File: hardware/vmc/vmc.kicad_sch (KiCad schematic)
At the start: 37 parts, among them J1 Conn_01x05_Pin, J2 push button, J3 BUS, M1 F130, Q1 BSS123, U1 SHT31-DIS, U2 PIC18F05Q40, U4 MCP2003B, U5 uA7805, U6 MAX22201

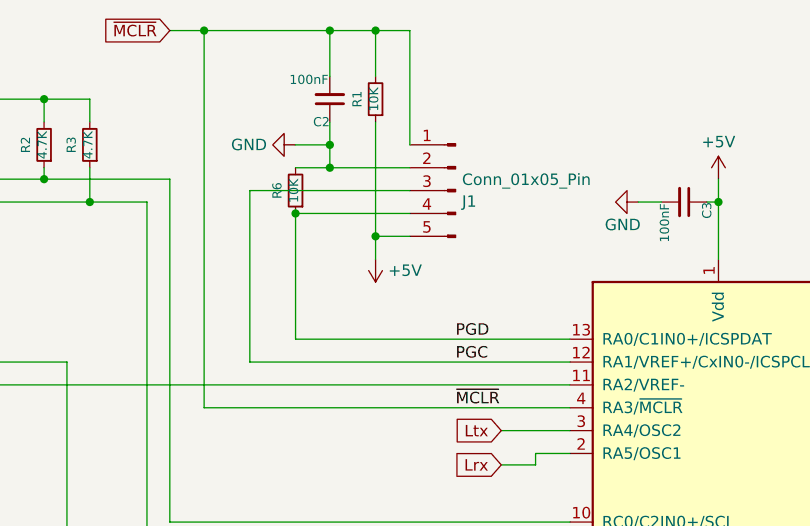
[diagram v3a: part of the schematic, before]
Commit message: vmc: update ICSP connector to match ventil
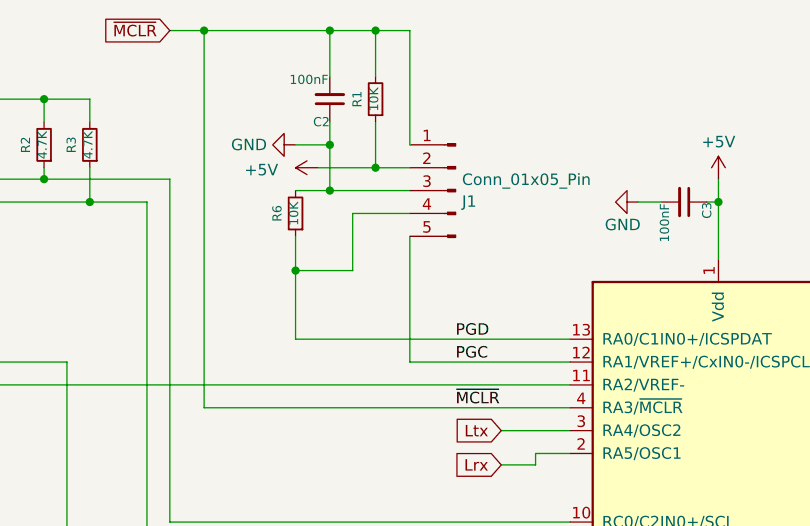
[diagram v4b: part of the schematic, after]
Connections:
- net +5V: now also J1.2 (Pin_2); no longer J1.5 (Pin_5)
- net GND: now also J1.3 (Pin_3); no longer J1.2 (Pin_2)
- net PGC: now also J1.5 (Pin_5); no longer J1.3 (Pin_3)
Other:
- moved on the sheet: R6
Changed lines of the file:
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@@
 	)
 	(junction
+		(at 201.93 38.1)
+		(diameter 0)
+		(color 0 0 0 0)
+	)
+	(junction
 		(at 73.66 161.29)
 		(diameter 0)
@@
 	)
 	(junction
-		(at 170.18 27.94)
+		(at 198.12 46.99)
 		(diameter 0)
 		(color 0 0 0 0)
 	)
 	(junction
-		(at 132.08 134.62)
+		(at 170.18 27.94)
 		(diameter 0)
 		(color 0 0 0 0)
 	)
 	(junction
-		(at 198.12 40.64)
+		(at 132.08 134.62)
 		(diameter 0)
 		(color 0 0 0 0)
@@
 	)
 	(junction
-		(at 207.01 43.18)
-		(diameter 0)
-		(color 0 0 0 0)
-	)
-	(junction
 		(at 86.36 161.29)
 		(diameter 0)
@@
 	)
 	(junction
-		(at 80.01 74.93)
+		(at 207.01 35.56)
 		(diameter 0)
 		(color 0 0 0 0)
 	)
 	(junction
-		(at 88.9 30.48)
+		(at 80.01 74.93)
 		(diameter 0)
 		(color 0 0 0 0)
 	)
 	(junction
-		(at 201.93 35.56)
+		(at 88.9 30.48)
 		(diameter 0)
 		(color 0 0 0 0)
@@
 	(wire
 		(pts
-			(xy 193.04 38.1) (xy 210.82 38.1)
-		)
-		(stroke
-			(width 0)
-			(type default)
-		)
-	)
-	(wire
-		(pts
 			(xy 86.36 161.29) (xy 86.36 163.83)
 		)
@@
 	(wire
 		(pts
-			(xy 193.04 57.15) (xy 193.04 38.1)
+			(xy 198.12 46.99) (xy 198.12 43.18)
 		)
 		(stroke
@@
 	(wire
 		(pts
-			(xy 210.82 43.18) (xy 207.01 43.18)
+			(xy 142.24 49.53) (xy 153.67 49.53)
 		)
 		(stroke
@@
 	(wire
 		(pts
-			(xy 142.24 49.53) (xy 153.67 49.53)
+			(xy 68.58 67.31) (xy 76.2 67.31)
 		)
 		(stroke
@@
 	(wire
 		(pts
-			(xy 68.58 67.31) (xy 76.2 67.31)
+			(xy 149.86 110.49) (xy 144.78 110.49)
 		)
 		(stroke
@@
 	(wire
 		(pts
-			(xy 149.86 110.49) (xy 144.78 110.49)
+			(xy 207.01 35.56) (xy 210.82 35.56)
 		)
 		(stroke
@@
 	(wire
 		(pts
-			(xy 198.12 54.61) (xy 198.12 40.64)
+			(xy 198.12 54.61) (xy 198.12 46.99)
 		)
 		(stroke
@@
 	(wire
 		(pts
+			(xy 204.47 40.64) (xy 204.47 46.99)
+		)
+		(stroke
+			(width 0)
+			(type default)
+		)
+	)
+	(wire
+		(pts
 			(xy 163.83 39.37) (xy 175.26 39.37)
 		)
@@
 	(wire
 		(pts
+			(xy 204.47 46.99) (xy 198.12 46.99)
+		)
+		(stroke
+			(width 0)
+			(type default)
+		)
+	)
+	(wire
+		(pts
 			(xy 109.22 53.34) (xy 111.76 53.34)
 		)
@@
 	(wire
 		(pts
-			(xy 228.6 57.15) (xy 193.04 57.15)
+			(xy 228.6 57.15) (xy 210.82 57.15)
 		)
 		(stroke
@@
 	(wire
 		(pts
+			(xy 201.93 38.1) (xy 210.82 38.1)
+		)
+		(stroke
+			(width 0)
+			(type default)
+		)
+	)
+	(wire
+		(pts
 			(xy 198.12 123.19) (xy 180.34 123.19)
 		)
@@
 	(wire
 		(pts
-			(xy 198.12 35.56) (xy 201.93 35.56)
+			(xy 198.12 38.1) (xy 201.93 38.1)
 		)
 		(stroke
@@
 	(wire
 		(pts
-			(xy 201.93 33.02) (xy 201.93 35.56)
+			(xy 201.93 33.02) (xy 201.93 38.1)
 		)
 		(stroke
@@
 	(wire
 		(pts
+			(xy 210.82 40.64) (xy 204.47 40.64)
+		)
+		(stroke
+			(width 0)
+			(type default)
+		)
+	)
+	(wire
+		(pts
 			(xy 142.24 72.39) (xy 152.4 72.39)
 		)
@@
 	(wire
 		(pts
-			(xy 207.01 30.48) (xy 207.01 43.18)
+			(xy 207.01 30.48) (xy 207.01 35.56)
 		)
 		(stroke
@@
 	(wire
 		(pts
-			(xy 228.6 80.01) (xy 172.72 80.01)
+			(xy 200.66 35.56) (xy 207.01 35.56)
 		)
 		(stroke
@@
 	(wire
 		(pts
-			(xy 76.2 46.99) (xy 88.9 46.99)
+			(xy 228.6 80.01) (xy 172.72 80.01)
 		)
 		(stroke
@@
 	(wire
 		(pts
-			(xy 198.12 40.64) (xy 210.82 40.64)
+			(xy 76.2 46.99) (xy 88.9 46.99)
 		)
 		(stroke
@@
 	(wire
 		(pts
-			(xy 201.93 35.56) (xy 210.82 35.56)
-		)
-		(stroke
-			(width 0)
-			(type default)
-		)
-	)
-	(wire
-		(pts
 			(xy 163.83 36.83) (xy 170.18 36.83)
 		)
@@
 	(wire
 		(pts
-			(xy 207.01 43.18) (xy 207.01 45.72)
+			(xy 238.76 39.37) (xy 236.22 39.37)
 		)
 		(stroke
@@
 	(wire
 		(pts
-			(xy 238.76 39.37) (xy 236.22 39.37)
+			(xy 162.56 120.65) (xy 162.56 123.19)
 		)
 		(stroke
@@
 	(wire
 		(pts
-			(xy 162.56 120.65) (xy 162.56 123.19)
+			(xy 210.82 43.18) (xy 210.82 57.15)
 		)
 		(stroke
@@
 	(symbol
 		(lib_id "Device:R_Small")
-		(at 198.12 38.1 180)
+		(at 198.12 40.64 180)
 		(unit 1)
 		(exclude_from_sim no)
@@
 		(dnp no)
 		(property "Reference" "R6"
-			(at 196.088 38.1 90)
+			(at 196.088 40.64 90)
 			(effects
 				(font
@@
 		)
 		(property "Value" "10K"
-			(at 197.9422 38.1254 90)
+			(at 197.9422 40.6654 90)
 			(effects
 				(font
@@
 		)
 		(property "Footprint" "Resistor_SMD:R_0805_2012Metric_Pad1.20x1.40mm_HandSolder"
-			(at 199.898 38.1 90)
+			(at 199.898 40.64 90)
 			(effects
 				(font
@@
 		)
 		(property "Datasheet" "~"
-			(at 198.12 38.1 0)
+			(at 198.12 40.64 0)
 			(effects
 				(font
@@
 		)
 		(property "Description" "Resistor, small symbol"
-			(at 198.12 38.1 0)
+			(at 198.12 40.64 0)
 			(effects
 				(font
@@
 		)
 		(property "P/N" "stock"
-			(at 198.12 38.1 0)
+			(at 198.12 40.64 0)
 			(effects
 				(font
@@
 	(symbol
 		(lib_id "power:+5V")
-		(at 207.01 45.72 180)
+		(at 200.66 35.56 90)
 		(unit 1)
 		(exclude_from_sim no)
@@
 		(on_board yes)
 		(dnp no)
-		(fields_autoplaced yes)
 		(property "Reference" "#PWR07"
-			(at 207.01 41.91 0)
+			(at 204.47 35.56 0)
 			(effects
 				(font
@@
 		)
 		(property "Value" "+5V"
-			(at 208.407 46.99 0)
+			(at 194.31 35.814 90)
 			(effects
 				(font
 					(size 1.27 1.27)
 				)
-				(justify right)
 			)
 		)
 		(property "Footprint" ""
-			(at 207.01 45.72 0)
+			(at 200.66 35.56 0)
 			(effects
 				(font
@@
 		)
 		(property "Datasheet" ""
-			(at 207.01 45.72 0)
+			(at 200.66 35.56 0)
 			(effects
 				(font
@@
 		)
 		(property "Description" "Power symbol creates a global label with name \"+5V\""
-			(at 207.01 45.72 0)
+			(at 200.66 35.56 0)
 			(effects
 				(font
@@
 		)
 		(property "P/N" ""
-			(at 207.01 45.72 0)
+			(at 200.66 35.56 0)
 			(effects
 				(font

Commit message: ventil, vmc: switch 7805 to a less expensive package
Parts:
- U5: footprint Package_TO_SOT_SMD:SOT-223-3_TabPin2 -> Package_TO_SOT_SMD:TO-252-3_TabPin2
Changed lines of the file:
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@@
 			)
 		)
-		(property "Footprint" "Package_TO_SOT_SMD:SOT-223-3_TabPin2"
+		(property "Footprint" "Package_TO_SOT_SMD:TO-252-3_TabPin2"
 			(at 106.045 165.1 0)
 			(effects

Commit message: hardware/vmc: convert a via to testpoint, so we can have a true PTH
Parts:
- added TP1: TestPoint, TestPoint:TestPoint_THTPad_D1.5mm_Drill0.7mm, symbol Connector:TestPoint
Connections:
- net +12V: now also TP1.1
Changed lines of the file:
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@@
+	(wire
+		(pts
+			(xy 73.66 158.75) (xy 73.66 161.29)
+		)
+		(stroke
+			(width 0)
+			(type default)
+		)
+	)
 	(wire
 		(pts
@@
 					(unit 1)
 				)
+			)
+		)
+	)
+	(symbol
+		(lib_id "Connector:TestPoint")
+		(at 73.66 158.75 0)
+		(unit 1)
+		(exclude_from_sim no)
+		(in_bom yes)
+		(on_board yes)
+		(dnp no)
+		(fields_autoplaced yes)
+		(property "Reference" "TP1"
+			(at 76.2 154.1779 0)
+			(effects
+				(font
+					(size 1.27 1.27)
+				)
+				(justify left)
+			)
+		)
+		(property "Value" "TestPoint"
+			(at 76.2 156.7179 0)
+			(effects
+				(font
+					(size 1.27 1.27)
+				)
+				(justify left)
+			)
+		)
+		(property "Footprint" "TestPoint:TestPoint_THTPad_D1.5mm_Drill0.7mm"
+			(at 78.74 158.75 0)
+			(effects
+				(font
+					(size 1.27 1.27)
+				)
+				(hide yes)
+			)
+		)
+		(property "Datasheet" "~"
+			(at 78.74 158.75 0)
+			(effects
+				(font
+					(size 1.27 1.27)
+				)
+				(hide yes)
+			)
+		)
+		(property "Description" "test point"
+			(at 73.66 158.75 0)
+			(effects
+				(font
+					(size 1.27 1.27)
+				)
+				(hide yes)
+			)
+		)
+		(pin "1"
+		)
+		(instances
+			(project ""
+				(path "/c1528490-5337-42d0-8cda-ee7adecf27aa"
+					(reference "TP1")
+					(unit 1)
+				)
